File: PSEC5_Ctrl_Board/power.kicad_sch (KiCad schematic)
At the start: 130 parts, among them U1 SIC473ED-T1-GE3, U23 SIC473ED-T1-GE3, U24 SIC473ED-T1-GE3, U25 SIC473ED-T1-GE3, U7 SIC473ED-T1-GE3

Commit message: minor changes
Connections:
- net GNDPWR: now also U1.10 (PGND), U1.11 (PGND), U1.17 (PGND), U1.30 (PGND), U1.9 (PGND), U23.10 (PGND), U23.11 (PGND), U23.17 (PGND), U23.30 (PGND), U23.9 (PGND), U24.10 (PGND), U24.11 (PGND), U24.17 (PGND), U24.30 (PGND), U24.9 (PGND), U25.10 (PGND), U25.11 (PGND), U25.17 (PGND), U25.30 (PGND), U25.9 (PGND), U7.10 (PGND), U7.11 (PGND), U7.17 (PGND), U7.30 (PGND), U7.9 (PGND)
- net 1V2 renamed VDD
- net 1V8 renamed VDD18
- net 2V5 renamed VDD25
- net 3V3 renamed VDD33
- net 5V renamed VDD50
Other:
- note added: "1.2V currently"

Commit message: Schematic is "done" ;( (999+ ERC errors)
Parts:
- removed C106, C118, C130, C142: 47u, Capacitor_SMD:C_0603_1608Metric, symbol Device:C_Small
- removed C107, C109, C112, C119, C121, C124, C131, C133, C136, C143, C145, C148: 0.1u, Capacitor_SMD:C_0603_1608Metric, symbol Device:C_Small
- removed C108, C120, C132, C144: 4.7u, Capacitor_SMD:C_0603_1608Metric, symbol Device:C_Small
- removed C110, C122, C134, C146: 2.2n, Capacitor_SMD:C_0603_1608Metric, symbol Device:C_Small
- removed C111, C123, C135, C147: 1.8n, Capacitor_SMD:C_0603_1608Metric, symbol Device:C_Small
- removed C113, C116, C125, C128, C137, C140, C149, C152: 64u, Capacitor_SMD:C_0603_1608Metric, symbol Device:C_Small
- removed C114, C126, C138, C150: 1u, Capacitor_SMD:C_0603_1608Metric, symbol Device:C_Small
- removed C115, C127, C139, C151: 33n, Capacitor_SMD:C_0603_1608Metric, symbol Device:C_Small
- removed C117, C129, C141, C153: 470p, Capacitor_SMD:C_0603_1608Metric, symbol Device:C_Small
- removed L2, L7, L8, L9: 4.7u, symbol Device:L_Small
- removed R55, R66, R77, R88: 560k, Resistor_SMD:R_0603_1608Metric, symbol Device:R_Small_US
- removed R56, R67, R78, R89: 3.3, Resistor_SMD:R_0603_1608Metric, symbol Device:R_Small_US
- removed R57, R68, R79, R90: 8.66k, Resistor_SMD:R_0603_1608Metric, symbol Device:R_Small_US
- removed R58, R69, R80, R91: 0R, Resistor_SMD:R_0603_1608Metric, symbol Device:R_Small_US
- removed R59, R70, R81, R92: 102k, Resistor_SMD:R_0603_1608Metric, symbol Device:R_Small_US
- removed R60: 31.3k, Resistor_SMD:R_0603_1608Metric, symbol Device:R_Small_US
- removed R61, R72, R83, R94: 232k, Resistor_SMD:R_0603_1608Metric, symbol Device:R_Small_US
- removed R62, R73, R84, R95: 2k, Resistor_SMD:R_0603_1608Metric, symbol Device:R_Small_US
- removed R63, R74, R85, R96: 60.4k, Resistor_SMD:R_0603_1608Metric, symbol Device:R_Small_US
- removed R64, R75, R86, R97: 52.3k, Resistor_SMD:R_0603_1608Metric, symbol Device:R_Small_US
- removed R65, R76, R87, R98: 10k, Resistor_SMD:R_0603_1608Metric, symbol Device:R_Small_US
- removed R71: 21.3k, Resistor_SMD:R_0603_1608Metric, symbol Device:R_Small_US
- removed R82: 12.5k, Resistor_SMD:R_0603_1608Metric, symbol Device:R_Small_US
- removed R93: 5k, Resistor_SMD:R_0603_1608Metric, symbol Device:R_Small_US
- removed R_EN_L1, R_EN_L2, R_EN_L3, R_EN_L4: DNP, Resistor_SMD:R_0603_1608Metric, symbol Device:R_Small_US
- removed U23, U24, U25, U7: SIC473ED-T1-GE3, PowerPAK_MLP55-27L_VIS, symbol PSEC5_ctrlbd:SIC473ED-T1-GE3
- added 1 (x2), 11, 111: LP38501TS-ADJ/NOPB, TS5B, symbol PSEC5_ctrlbd:LP38501TS-ADJ_NOPB
- added J1: 1766343, CONN_1766343_PXC, symbol PSEC5_ctrlbd:1766343
- added R32, R33, R35, R36, R38, R40, R41, R43: 10k, Resistor_SMD:R_0603_1608Metric, symbol Device:R_Small_US
- added R34: 44.5k, Resistor_SMD:R_0603_1608Metric, symbol Device:R_Small_US
- added R37, R39: 31.3k, Resistor_SMD:R_0603_1608Metric, symbol Device:R_Small_US
- added R42: 9.83k, Resistor_SMD:R_0603_1608Metric, symbol Device:R_Small_US
- added TP1, TP3, TP5, TP7: GND, symbol Connector:TestPoint
- added TP17: 5V_PGOOD, symbol Connector:TestPoint
- added TP18: 5V_BUCK, symbol Connector:TestPoint
- added TP2: 3V3_DUT, symbol Connector:TestPoint
- added TP4: 2V5_DUT, symbol Connector:TestPoint
- added TP6: 1V8_DUT, symbol Connector:TestPoint
- added TP8: 1V2_DUT, symbol Connector:TestPoint
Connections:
- net GND: now also 1.3 (GND), 1.3 (GND), 1.6 (TAB), 1.6 (TAB), 11.3 (GND), 11.6 (TAB), 111.3 (GND), 111.6 (TAB), R33.2, R36.2, R40.2, R43.2, TP1.1, TP3.1, TP5.1, TP7.1
- net PGOOD renamed 5V_PGOOD
- net 5V_PGOOD: now also TP17.1
- net VDD50 renamed VDD_BUCK_5V
- net VDD_BUCK_5V: now also 1.1 (EN), 1.1 (EN), 1.2 (IN), 1.2 (IN), 11.1 (EN), 11.2 (IN), 111.1 (EN), 111.2 (IN), R32.1, R32.2, R35.1, R35.2, R38.1, R38.2, R41.1, R41.2, TP18.1
- net Vin: no longer names the net of C1.1, C6.1, R9.1, U1.1 (VCIN), U1.29 (VIN), U1.7 (VIN), U1.8 (VIN)
- net Vin: now also J1.1
- new net: 1.5 (ADJ), R36.1, R37.2
- new net: 111.5 (ADJ), R42.2, R43.1
- new net: 1.5 (ADJ), R33.1, R34.2
- new net: 11.5 (ADJ), R39.2, R40.1
- new net 1V2_DUT: 111.4 (OUT), R42.1, TP8.1
- new net 1V8_DUT: 11.4 (OUT), R39.1, TP6.1
- new net 2V5_DUT: 1.4 (OUT), R37.1, TP4.1
- new net 3V3_DUT: 1.4 (OUT), R34.1, TP2.1
- no-connect marks 0 -> 2
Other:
- note added: "1V2 to DUT"
- note added: "1V8 to DUT"
- note added: "2V5 to DUT"
- note added: "3V3 to DUT"
- note added: "5V Buck Supply to Kria Also power into LDO's"
- note added: "Physical Connector (Plug) 6V-55V"
- note added: "Vmin = 1.586V Vtyp = 1.200V Vmax = 1.249V"
- note added: "Vmin = 1.735V Vtyp = 1.798V Vmax = 1.874V"
- note added: "Vmin = 2.413V Vtyp = 2.500V Vmax = 2.588V"
- note added: "Vmin = 3.19V Vtyp = 3.30V Vmax = 3.435V"
- note removed: "1.2V Power Rail"
- note removed: "1.2V currently"
- note removed: "1.8V Power Rail"
- note removed: "2.5V Power Rail"
- note removed: "3.3V Power Rail"
- note removed: "5V Power Rail"
- note removed: "Vin (6V-55V)"

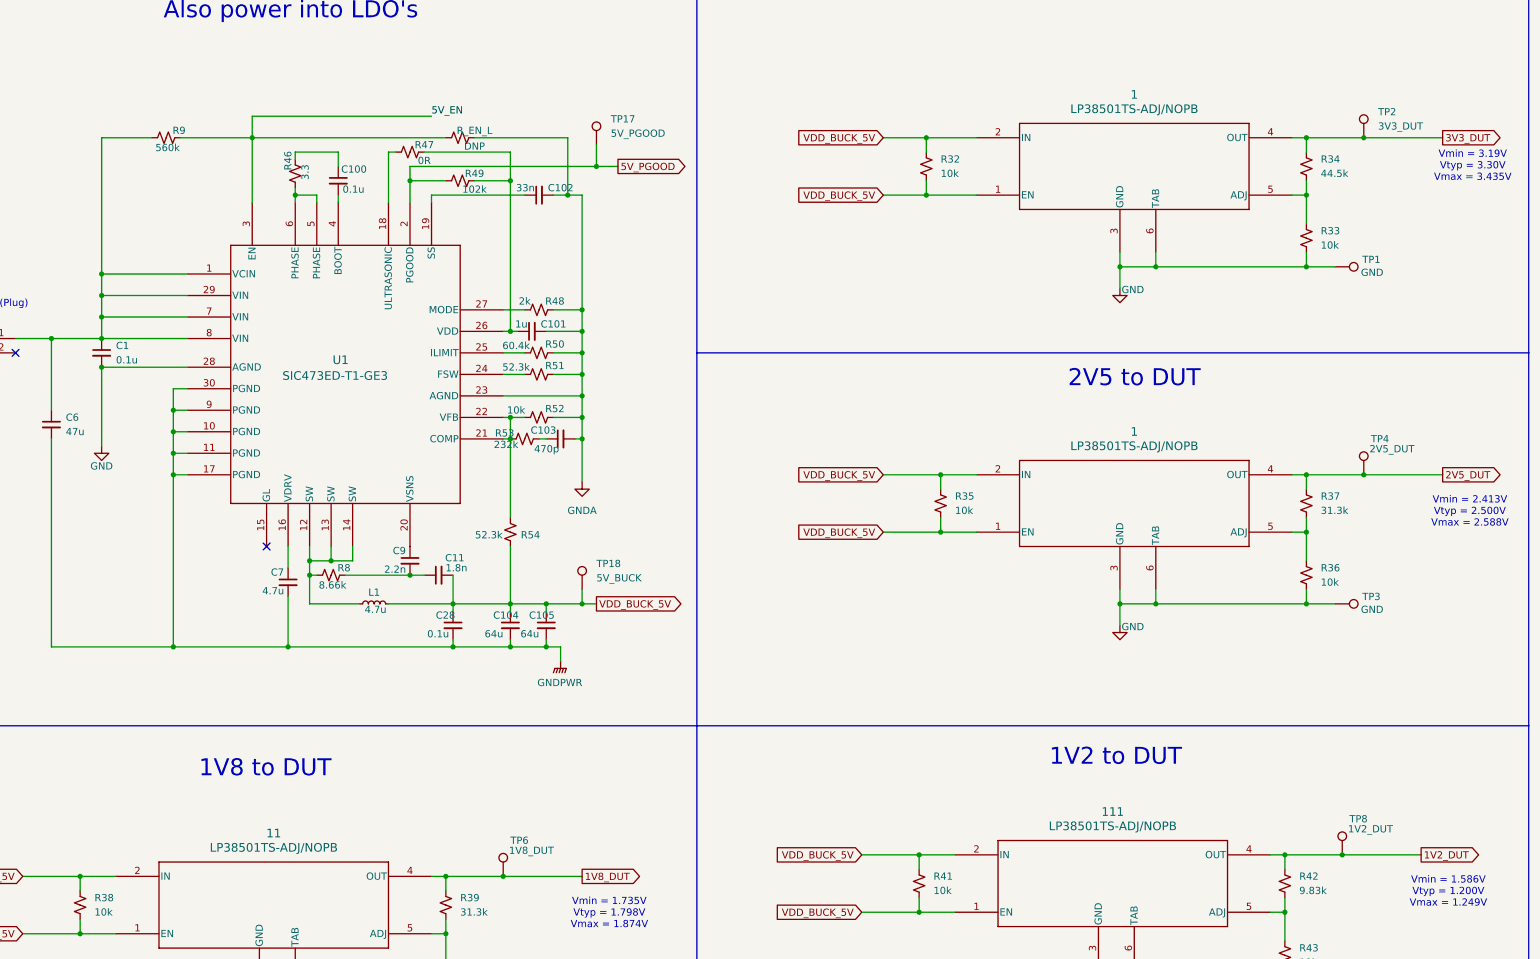
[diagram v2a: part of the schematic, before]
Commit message: changes to schematic errors
Errors should be closer to 897~
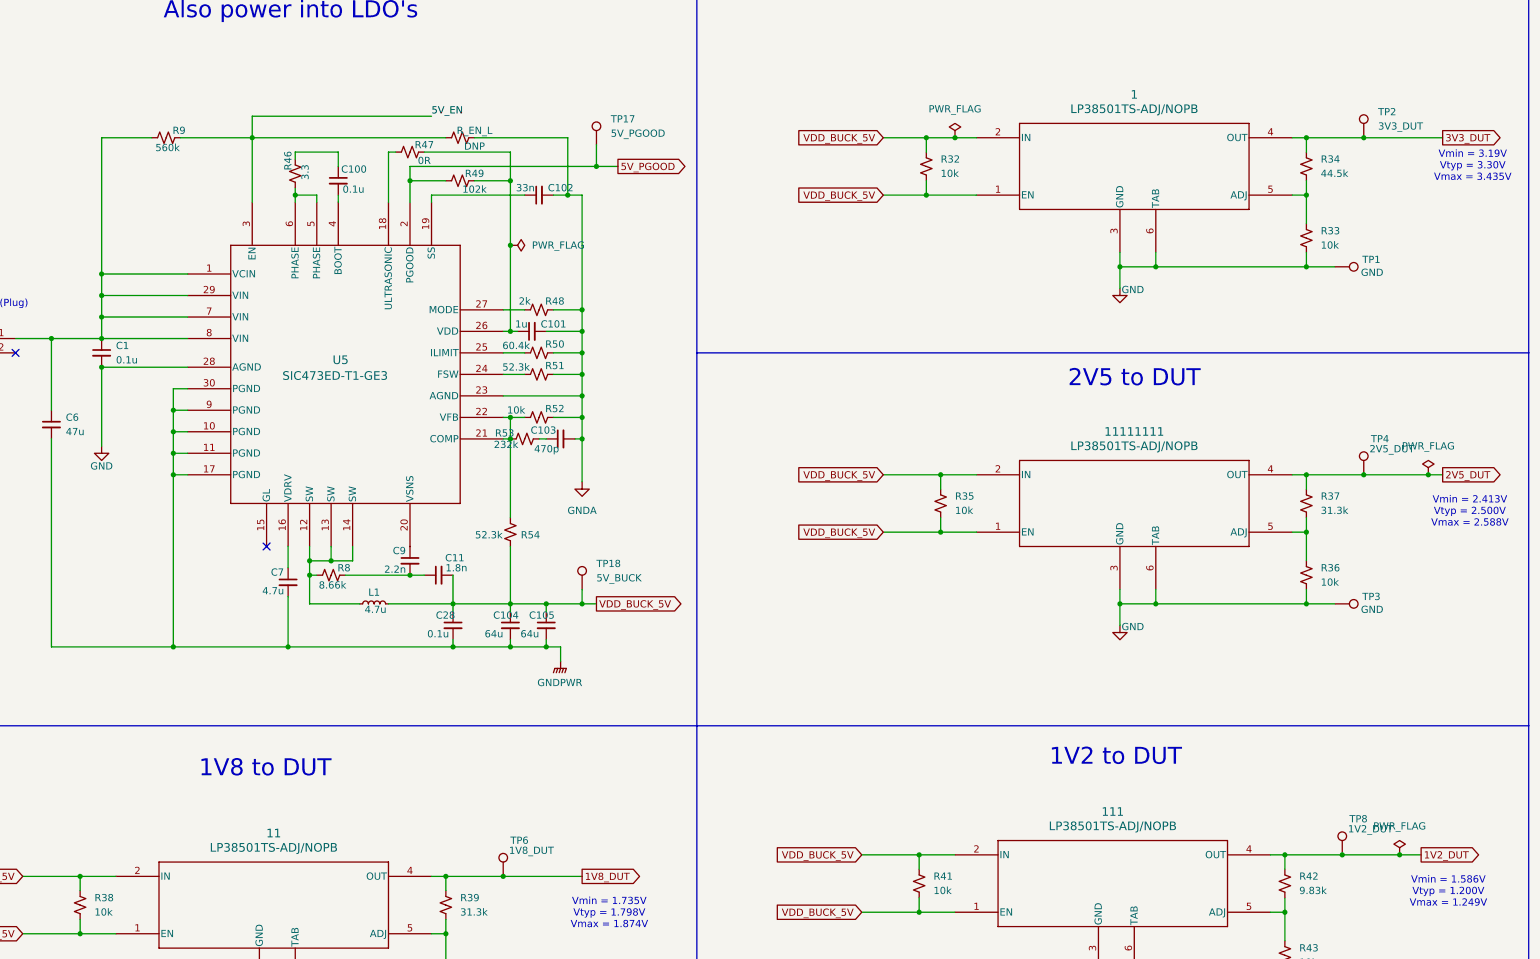
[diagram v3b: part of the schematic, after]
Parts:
- removed 1: LP38501TS-ADJ/NOPB, TS5B, symbol PSEC5_ctrlbd:LP38501TS-ADJ_NOPB
- removed U1: SIC473ED-T1-GE3, PowerPAK_MLP55-27L_VIS, symbol PSEC5_ctrlbd:SIC473ED-T1-GE3
- added 11111111: LP38501TS-ADJ/NOPB, TS5B, symbol PSEC5_ctrlbd:LP38501TS-ADJ_NOPB
- added U5: SIC473ED-T1-GE3, PowerPAK_MLP55-27L_VIS, symbol PSEC5_ctrlbd:SIC473ED-T1-GE3
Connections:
- net 2V5_DUT: now also 11111111.4 (OUT)
- net 5V_EN: now also U5.3 (EN)
- net 5V_PGOOD: now also U5.2 (PGOOD)
- net GND: now also 11111111.3 (GND), 11111111.6 (TAB), U5.28 (AGND)
- net GNDA: now also U5.23 (AGND)
- net GNDPWR: now also U5.10 (PGND), U5.11 (PGND), U5.17 (PGND), U5.30 (PGND), U5.9 (PGND)
- net VDD_BUCK_5V: now also 11111111.1 (EN), 11111111.2 (IN)
- net at R46.1: now also U5.5 (PHASE), U5.6 (PHASE)
- net at R51.1: now also U5.24 (FSW)
- net at R52.1, R53.1, R54.2: now also U5.21 (COMP), U5.22 (VFB)
- net at R36.1, R37.2: now also 11111111.5 (ADJ)
- net at C1.1, C6.1, J1.1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: now also U5.1 (VCIN), U5.29 (VIN), U5.7 (VIN), U5.8 (VIN)
- net at C101.1, R47.1, R49.1: now also U5.26 (VDD)
- net at R47.2: now also U5.18 (ULTRASONIC)
- net at C100.2: now also U5.4 (BOOT)
- net at R48.1: now also U5.27 (MODE)
- net at C7.1: now also U5.16 (VDRV)
- net at L1.1, R8.1: now also U5.12 (SW), U5.13 (SW), U5.14 (SW)
- net at C102.1: now also U5.19 (SS)
- net at C9.1: now also U5.20 (VSNS)
- net at R50.1: now also U5.25 (ILIMIT)

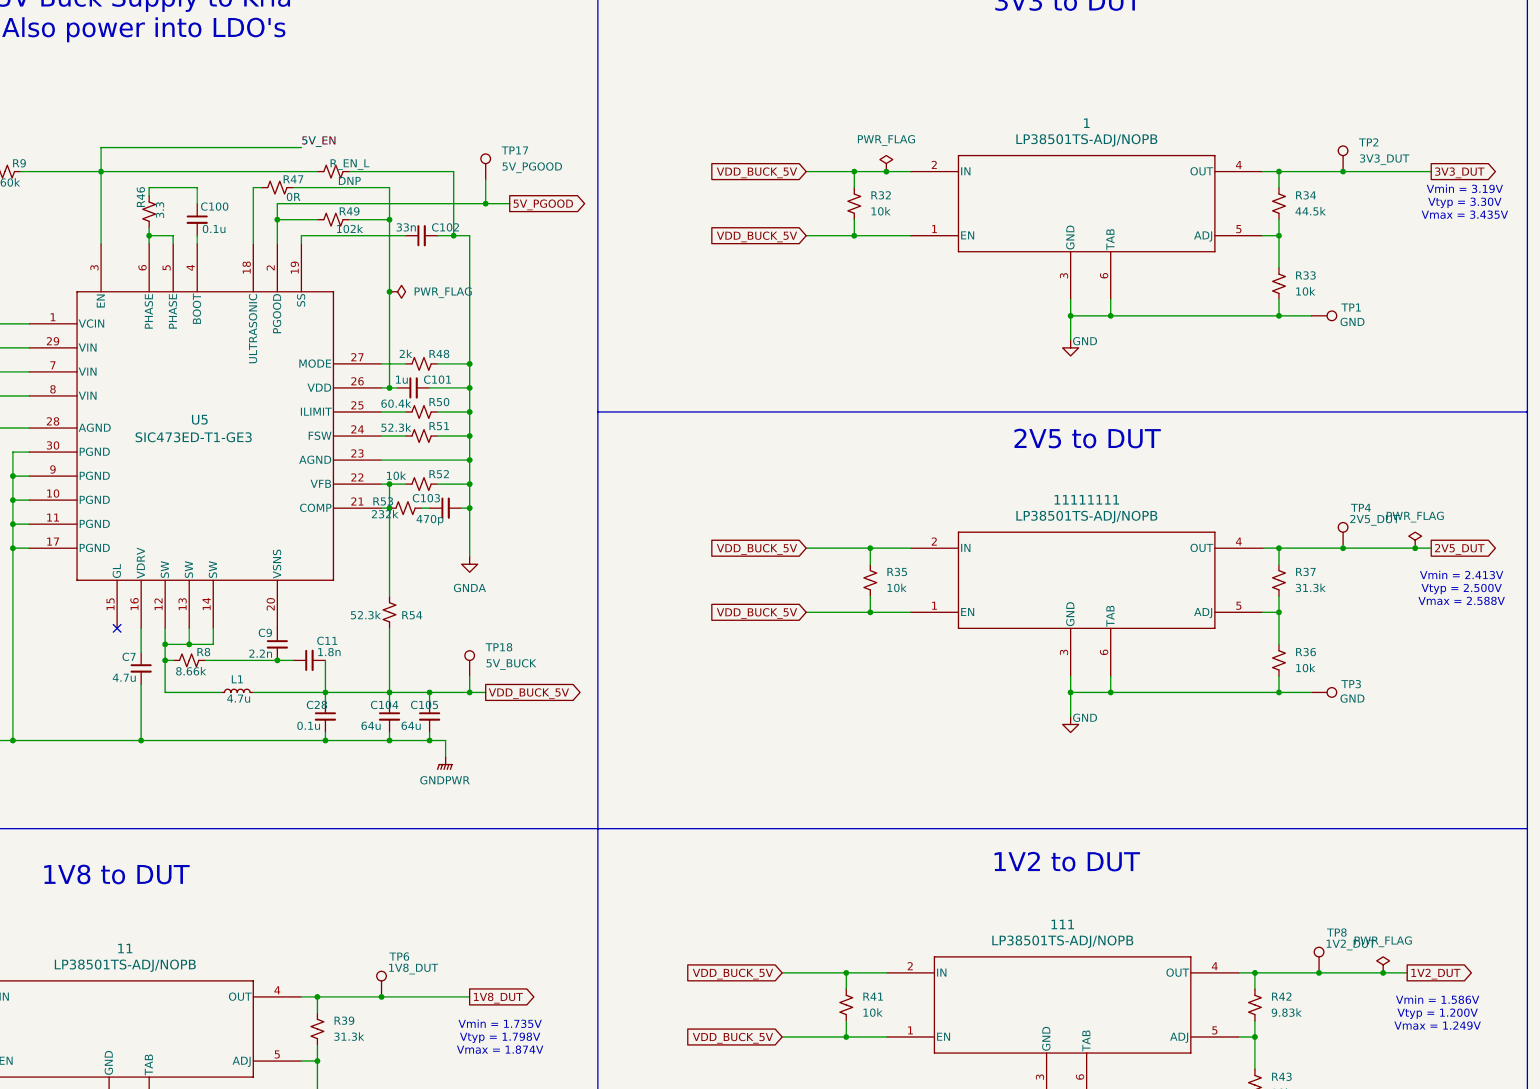
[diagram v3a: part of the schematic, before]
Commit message: Deleted some Pages, still lots of errors :(
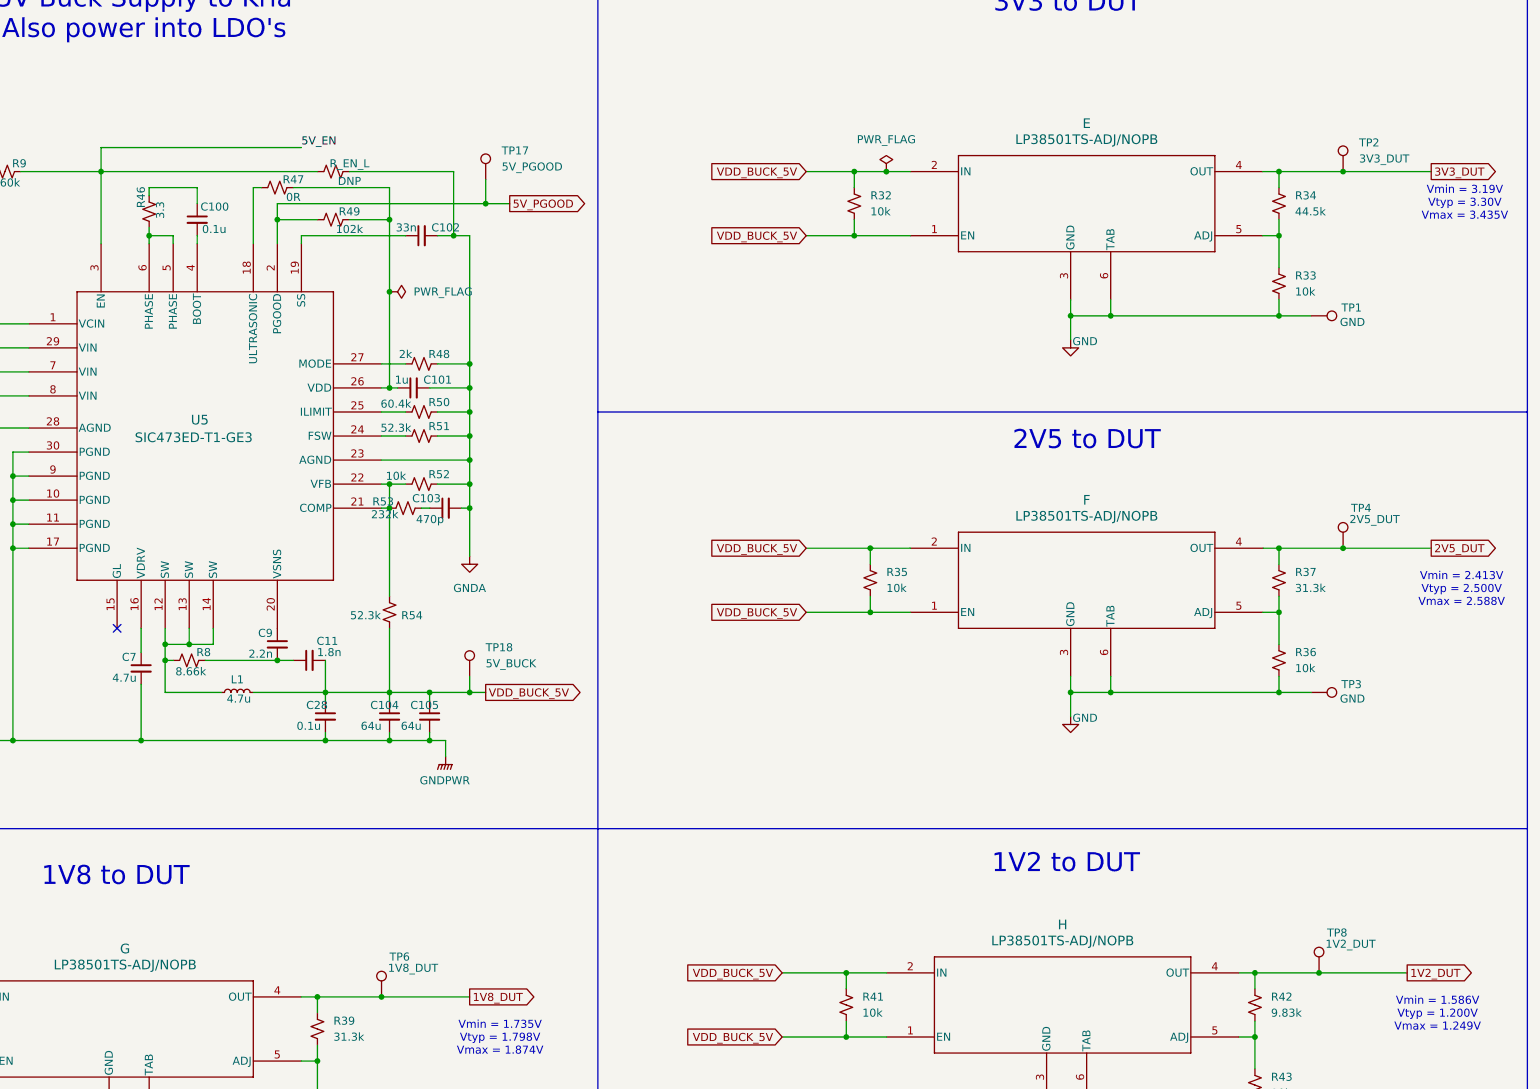
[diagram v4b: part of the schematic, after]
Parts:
- removed 1, 11, 111, 11111111: LP38501TS-ADJ/NOPB, TS5B, symbol PSEC5_ctrlbd:LP38501TS-ADJ_NOPB
- added E, F, G, H: LP38501TS-ADJ/NOPB, TS5B, symbol PSEC5_ctrlbd:LP38501TS-ADJ_NOPB
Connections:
- net 1V2_DUT: now also H.4 (OUT)
- net 1V8_DUT: now also G.4 (OUT)
- net 2V5_DUT: now also F.4 (OUT)
- net 3V3_DUT: now also E.4 (OUT)
- net GND: now also E.3 (GND), E.6 (TAB), F.3 (GND), F.6 (TAB), G.3 (GND), G.6 (TAB), H.3 (GND), H.6 (TAB)
- net VDD_BUCK_5V: now also E.1 (EN), E.2 (IN), F.1 (EN), F.2 (IN), G.1 (EN), G.2 (IN), H.1 (EN), H.2 (IN)
- net at R36.1, R37.2: now also F.5 (ADJ)
- net at R42.2, R43.1: now also H.5 (ADJ)
- net at R33.1, R34.2: now also E.5 (ADJ)
- net at R39.2, R40.1: now also G.5 (ADJ)

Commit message: Minor Schematic Changes, ERC still haunts me :(
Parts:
- added C10, C12, C13, C8: 10u, Capacitor_SMD:C_0603_1608Metric, symbol Device:C_Small
- R39: value 31.3k -> 19.7k
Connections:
- net GND: now also C10.2, C12.2, C13.2, C8.2
- net VDD_BUCK_5V: now also C10.1, C12.1, C13.1, C8.1

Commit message: Some more Changes
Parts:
- added C17: 10u, Capacitor_SMD:C_0603_1608Metric, symbol Device:C_Small
- added E2: LP38501TS-ADJ/NOPB, TS5B, symbol PSEC5_ctrlbd:LP38501TS-ADJ_NOPB
- added R25, R30: 10k, Resistor_SMD:R_0603_1608Metric, symbol Device:R_Small_US
- added R29: 44.5k, Resistor_SMD:R_0603_1608Metric, symbol Device:R_Small_US
- added TP27: GND, symbol Connector:TestPoint
- added TP28: 3V3_FEED, symbol Connector:TestPoint
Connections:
- net GND: now also C17.2, E2.3 (GND), E2.6 (TAB), R30.2, TP27.1
- net VDD_BUCK_5V: now also C17.1, E2.1 (EN), E2.2 (IN), R25.1, R25.2
- new net: E2.5 (ADJ), R29.2, R30.1
- new net 3V3_FEED: E2.4 (OUT), R29.1, TP28.1
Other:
- note added: "3V3 Feed to LDO's"
